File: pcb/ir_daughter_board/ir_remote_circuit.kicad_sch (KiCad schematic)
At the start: 12 parts, among them J2 Conn_01x12, J3 Conn_01x12, SW1 BOOT, SW2 RESET, U2 ESP32-WROOM-32E_(16MB)

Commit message: minor editorial changes
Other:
- moved on the sheet: C10, C9, D6, J2, J3, R8, R9, SW1, SW2

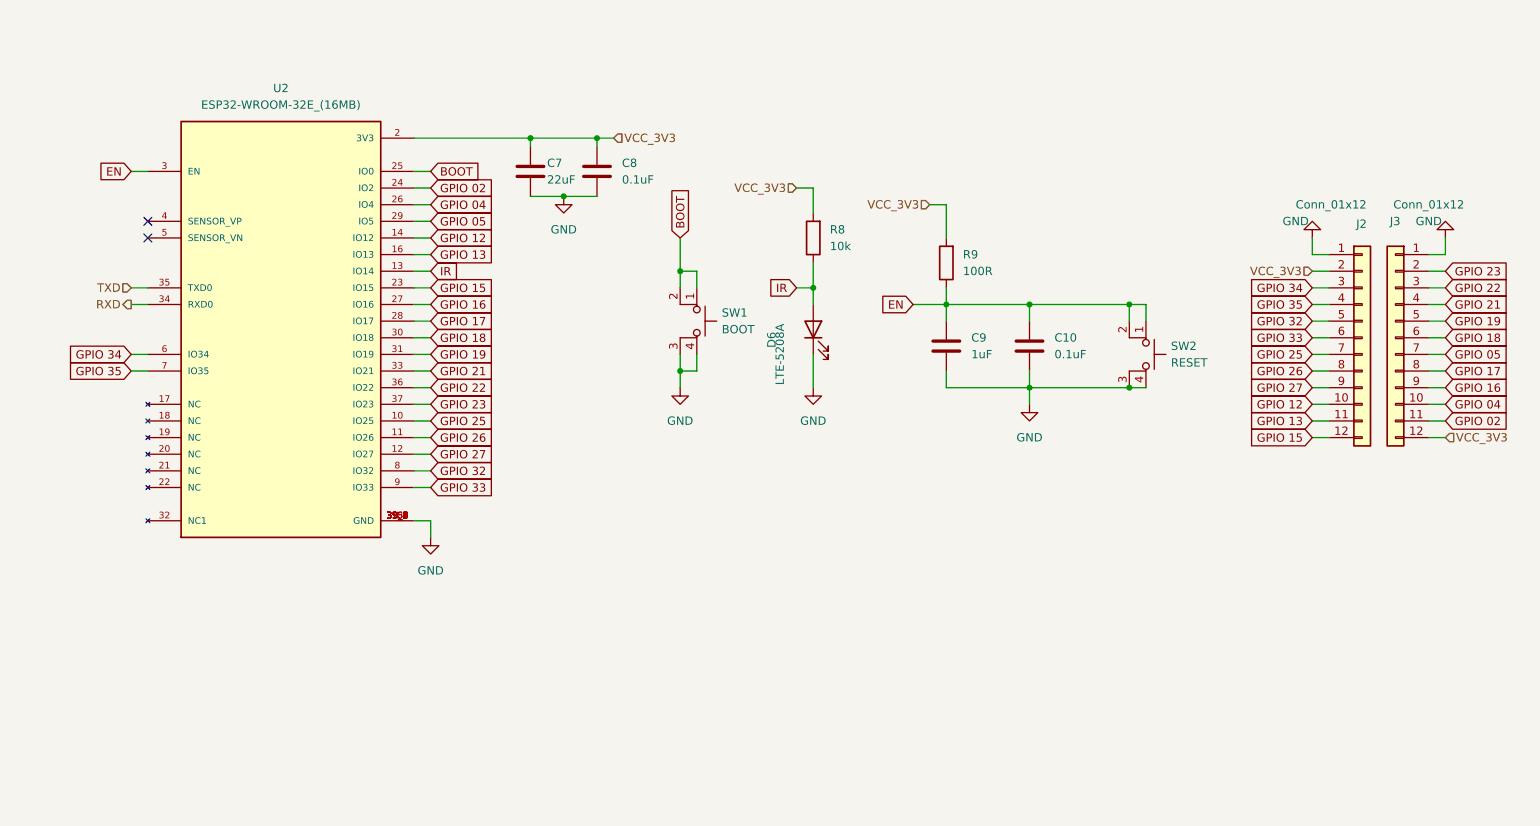
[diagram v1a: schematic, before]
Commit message: refined circuit with reddit comments
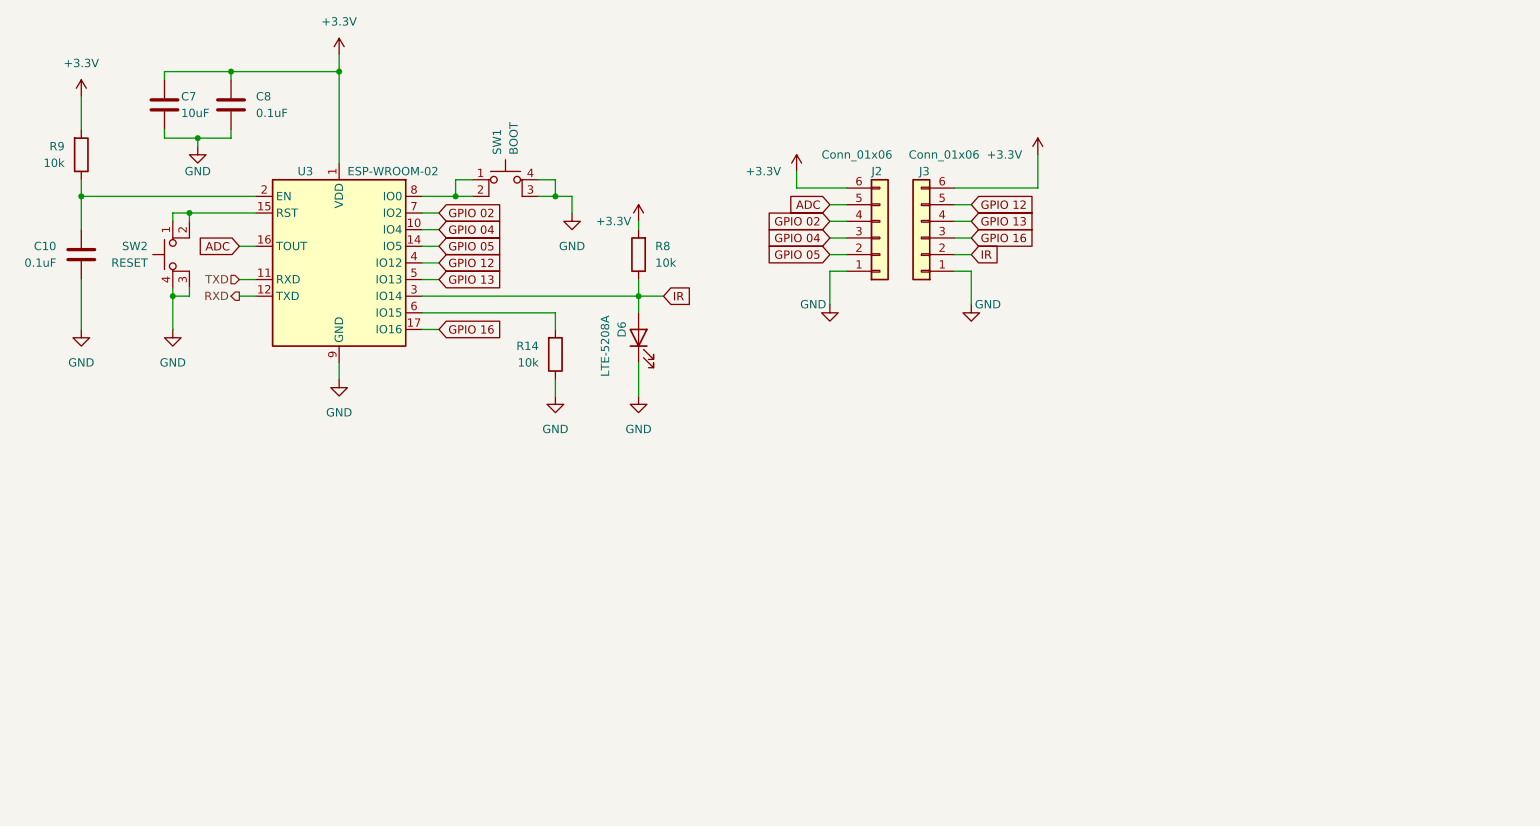
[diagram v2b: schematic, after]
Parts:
- removed C9: 1uF, Capacitor_SMD:C_0603_1608Metric, symbol Device:C
- removed J2, J3: Conn_01x12, Connector_PinHeader_2.54mm:PinHeader_1x12_P2.54mm_Vertical, symbol Connector_Generic:Conn_01x12
- removed U2: ESP32-WROOM-32E_(16MB), ESP32-WROOM-32E:MODULE_ESP32-WROOM-32E_(16MB), symbol ESP32-WROOM-32E:ESP32-WROOM-32E_(16MB)
- added J2, J3: Conn_01x06, Connector_PinHeader_2.54mm:PinHeader_1x06_P2.54mm_Vertical, symbol Connector_Generic:Conn_01x06
- added R14: 10k, Resistor_SMD:R_0603_1608Metric, symbol Device:R
- added U3: ESP-WROOM-02, RF_Module:ESP-WROOM-02, symbol RF_Module:ESP-WROOM-02
- C7: value 22uF -> 10uF
- R9: value 100R -> 10k
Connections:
- net GND: now also J2.1 (Pin_1), J3.1 (Pin_1), R14.1, U3.13 (GND), U3.18 (GND), U3.19 (GND), U3.9 (GND)
- net GPIO 02: now also J2.4 (Pin_4), U3.7 (IO2)
- net GPIO 04: now also J2.3 (Pin_3), U3.10 (IO4)
- net GPIO 05: now also J2.2 (Pin_2), U3.14 (IO5)
- net GPIO 12: now also J3.5 (Pin_5), U3.4 (IO12)
- net GPIO 13: now also J3.4 (Pin_4), U3.5 (IO13)
- net GPIO 16: now also J3.3 (Pin_3), U3.17 (IO16)
- net IR: now also J3.2 (Pin_2), U3.3 (IO14)
- net RXD: now also U3.12 (TXD)
- net TXD: now also U3.11 (RXD)
- net BOOT: no longer names the net of SW1.1, SW1.2
- net BOOT: now also U3.8 (IO0)
- net EN: no longer names the net of C10.1, R9.1
- net EN: now also U3.2 (EN); no longer SW2.1, SW2.2
- net VCC_3V3 renamed +3V3
- net +3V3: now also J2.6 (Pin_6), J3.6 (Pin_6), U3.1 (VDD)
- new net: SW2.1, SW2.2, U3.15 (RST)
- new net: R14.2, U3.6 (IO15)
- new net ADC: J2.5 (Pin_5), U3.16 (TOUT)
- no-connect marks 2 -> 0
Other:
- moved on the sheet: C10, C7, C8, D6, R8, R9, SW1, SW2

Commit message: updated schematic
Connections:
- net ADC: now also J3.3 (Pin_3); no longer J2.5 (Pin_5)
- net GND: no longer D6.1 (K)
- net GPIO 02: now also J2.5 (Pin_5); no longer J2.4 (Pin_4)
- net GPIO 04: now also J3.5 (Pin_5); no longer J2.3 (Pin_3)
- net GPIO 05: now also J3.4 (Pin_4); no longer J2.2 (Pin_2)
- net GPIO 12: now also J2.3 (Pin_3); no longer J3.5 (Pin_5)
- net GPIO 13: now also J2.4 (Pin_4); no longer J3.4 (Pin_4)
- net GPIO 16: now also J3.2 (Pin_2); no longer J3.3 (Pin_3)
- net IR: now also D6.1 (K), J2.2 (Pin_2); no longer D6.2 (A), J3.2 (Pin_2), R8.1
- new net: D6.2 (A), R8.1
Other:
- moved on the sheet: D6, R8

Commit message: minor update in PCB
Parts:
- C10, C8: value 0.1uF -> 100nF
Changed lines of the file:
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@@
   )
   (symbol (lib_id "Device:C") (at 48.26 81.28 0) (mirror y) (unit 1)
-    (in_bom yes) (on_board yes) (fields_autoplaced)
-    (property "Reference" "C10" (id 0) (at 44.45 80.0099 0)
-      (effects (font (size 1.27 1.27)) (justify left))
+    (in_bom yes) (on_board yes)
+    (property "Reference" "C10" (id 0) (at 41.275 80.01 0)
+      (effects (font (size 1.27 1.27)) (justify right))
     )
-    (property "Value" "0.1uF" (id 1) (at 44.45 82.5499 0)
-      (effects (font (size 1.27 1.27)) (justify left))
+    (property "Value" "100nF" (id 1) (at 39.37 82.55 0)
+      (effects (font (size 1.27 1.27)) (justify right))
     )
     (property "Footprint" "Capacitor_SMD:C_0603_1608Metric" (id 2) (at 47.2948 85.09 0)
@@
       (effects (font (size 1.27 1.27)) (justify left))
     )
-    (property "Value" "0.1uF" (id 1) (at 74.93 59.6899 0)
+    (property "Value" "100nF" (id 1) (at 74.93 59.6899 0)
       (effects (font (size 1.27 1.27)) (justify left))
     )

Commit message: minor updateds in references and values
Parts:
- D5: renamed from D6; value LTE-5208A -> IR-LED 940nm
- SW1: renamed from SW2; value RESET -> SW_MEC_5E
- SW2: renamed from SW1; value BOOT -> SW_MEC_5E
- renumbered C10 to C7, C7 to C8, C8 to C9, R9 to R11, R14 to R12, R8 to R13, U3 to U2
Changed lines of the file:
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@@
   (symbol (lib_id "power:+3.3V") (at 48.26 57.15 0) (unit 1)
     (in_bom yes) (on_board yes) (fields_autoplaced)
-    (property "Reference" "#PWR018" (id 0) (at 48.26 60.96 0)
+    (property "Reference" "#PWR020" (id 0) (at 48.26 60.96 0)
       (effects (font (size 1.27 1.27)) hide)
     )
@@
   (symbol (lib_id "power:GND") (at 48.26 92.71 0) (mirror y) (unit 1)
     (in_bom yes) (on_board yes) (fields_autoplaced)
-    (property "Reference" "#PWR012" (id 0) (at 48.26 99.06 0)
+    (property "Reference" "#PWR021" (id 0) (at 48.26 99.06 0)
       (effects (font (size 1.27 1.27)) hide)
     )
@@
   (symbol (lib_id "Device:C") (at 48.26 81.28 0) (mirror y) (unit 1)
     (in_bom yes) (on_board yes)
-    (property "Reference" "C10" (id 0) (at 41.275 80.01 0)
+    (property "Reference" "C7" (id 0) (at 41.275 80.01 0)
       (effects (font (size 1.27 1.27)) (justify right))
     )
@@
   (symbol (lib_id "Device:R") (at 133.35 69.85 180) (unit 1)
     (in_bom yes) (on_board yes) (fields_autoplaced)
-    (property "Reference" "R8" (id 0) (at 135.89 68.5799 0)
+    (property "Reference" "R13" (id 0) (at 135.89 68.5799 0)
       (effects (font (size 1.27 1.27)) (justify right))
     )
@@
   (symbol (lib_id "power:+3.3V") (at 194.31 66.04 0) (unit 1)
     (in_bom yes) (on_board yes)
-    (property "Reference" "#PWR024" (id 0) (at 194.31 69.85 0)
+    (property "Reference" "#PWR032" (id 0) (at 194.31 69.85 0)
       (effects (font (size 1.27 1.27)) hide)
     )
@@
   (symbol (lib_id "Device:R") (at 48.26 66.04 0) (mirror x) (unit 1)
     (in_bom yes) (on_board yes) (fields_autoplaced)
-    (property "Reference" "R9" (id 0) (at 45.72 64.7699 0)
+    (property "Reference" "R11" (id 0) (at 45.72 64.7699 0)
       (effects (font (size 1.27 1.27)) (justify right))
     )
@@
   )
   (symbol (lib_id "Switch:SW_MEC_5E") (at 64.77 81.28 90) (mirror x) (unit 1)
-    (in_bom yes) (on_board yes) (fields_autoplaced)
-    (property "Reference" "SW2" (id 0) (at 58.42 80.0099 90)
-      (effects (font (size 1.27 1.27)) (justify left))
-    )
-    (property "Value" "RESET" (id 1) (at 58.42 82.5499 90)
-      (effects (font (size 1.27 1.27)) (justify left))
+    (in_bom yes) (on_board yes)
+    (property "Reference" "SW1" (id 0) (at 55.88 80.01 90)
+      (effects (font (size 1.27 1.27)) (justify right))
+    )
+    (property "Value" "SW_MEC_5E" (id 1) (at 58.42 92.71 0)
+      (effects (font (size 1.27 1.27)) (justify right))
     )
     (property "Footprint" "Button_Switch_SMD:SW_SPST_Omron_B3FS-100xP" (id 2) (at 57.15 81.28 0)
@@
   (symbol (lib_id "Switch:SW_MEC_5E") (at 113.03 72.39 0) (unit 1)
     (in_bom yes) (on_board yes) (fields_autoplaced)
-    (property "Reference" "SW1" (id 0) (at 111.7599 66.04 90)
-      (effects (font (size 1.27 1.27)) (justify left))
-    )
-    (property "Value" "BOOT" (id 1) (at 114.2999 66.04 90)
-      (effects (font (size 1.27 1.27)) (justify left))
-    )
+    (property "Reference" "SW2" (id 0) (at 113.03 62.23 0))
+    (property "Value" "SW_MEC_5E" (id 1) (at 113.03 64.77 0))
     (property "Footprint" "Button_Switch_SMD:SW_SPST_Omron_B3FS-100xP" (id 2) (at 113.03 64.77 0)
       (effects (font (size 1.27 1.27)) hide)
@@
   (symbol (lib_id "Device:C") (at 71.12 58.42 0) (unit 1)
     (in_bom yes) (on_board yes) (fields_autoplaced)
-    (property "Reference" "C8" (id 0) (at 74.93 57.1499 0)
+    (property "Reference" "C9" (id 0) (at 74.93 57.1499 0)
       (effects (font (size 1.27 1.27)) (justify left))
     )
@@
   (symbol (lib_id "power:GND") (at 123.19 74.93 0) (unit 1)
     (in_bom yes) (on_board yes) (fields_autoplaced)
-    (property "Reference" "#PWR010" (id 0) (at 123.19 81.28 0)
+    (property "Reference" "#PWR027" (id 0) (at 123.19 81.28 0)
       (effects (font (size 1.27 1.27)) hide)
     )
@@
   (symbol (lib_id "power:+3.3V") (at 157.48 68.58 0) (unit 1)
     (in_bom yes) (on_board yes)
-    (property "Reference" "#PWR019" (id 0) (at 157.48 72.39 0)
+    (property "Reference" "#PWR029" (id 0) (at 157.48 72.39 0)
       (effects (font (size 1.27 1.27)) hide)
     )
@@
   (symbol (lib_id "Device:R") (at 120.65 96.52 0) (mirror x) (unit 1)
     (in_bom yes) (on_board yes) (fields_autoplaced)
-    (property "Reference" "R14" (id 0) (at 118.11 95.2499 0)
+    (property "Reference" "R12" (id 0) (at 118.11 95.2499 0)
       (effects (font (size 1.27 1.27)) (justify right))
     )
@@
   (symbol (lib_id "power:GND") (at 66.04 64.77 0) (unit 1)
     (in_bom yes) (on_board yes)
-    (property "Reference" "#PWR0102" (id 0) (at 66.04 71.12 0)
+    (property "Reference" "#PWR023" (id 0) (at 66.04 71.12 0)
       (effects (font (size 1.27 1.27)) hide)
     )
@@
   (symbol (lib_id "Device:C") (at 60.96 58.42 0) (unit 1)
     (in_bom yes) (on_board yes)
-    (property "Reference" "C7" (id 0) (at 63.5 57.15 0)
+    (property "Reference" "C8" (id 0) (at 63.5 57.15 0)
       (effects (font (size 1.27 1.27)) (justify left))
     )
@@
   (symbol (lib_id "power:GND") (at 120.65 102.87 0) (unit 1)
     (in_bom yes) (on_board yes) (fields_autoplaced)
-    (property "Reference" "#PWR020" (id 0) (at 120.65 109.22 0)
+    (property "Reference" "#PWR026" (id 0) (at 120.65 109.22 0)
       (effects (font (size 1.27 1.27)) hide)
     )
@@
   (symbol (lib_id "power:GND") (at 87.63 100.33 0) (unit 1)
     (in_bom yes) (on_board yes) (fields_autoplaced)
-    (property "Reference" "#PWR0101" (id 0) (at 87.63 106.68 0)
+    (property "Reference" "#PWR025" (id 0) (at 87.63 106.68 0)
       (effects (font (size 1.27 1.27)) hide)
     )
@@
   (symbol (lib_id "power:+3.3V") (at 87.63 50.8 0) (unit 1)
     (in_bom yes) (on_board yes) (fields_autoplaced)
-    (property "Reference" "#PWR021" (id 0) (at 87.63 54.61 0)
+    (property "Reference" "#PWR024" (id 0) (at 87.63 54.61 0)
       (effects (font (size 1.27 1.27)) hide)
     )
@@
   (symbol (lib_id "power:GND") (at 162.56 88.9 0) (mirror y) (unit 1)
     (in_bom yes) (on_board yes)
-    (property "Reference" "#PWR013" (id 0) (at 162.56 95.25 0)
+    (property "Reference" "#PWR030" (id 0) (at 162.56 95.25 0)
       (effects (font (size 1.27 1.27)) hide)
     )
@@
   (symbol (lib_id "Device:LED") (at 133.35 81.28 90) (unit 1)
     (in_bom yes) (on_board yes)
-    (property "Reference" "D6" (id 0) (at 130.81 80.01 0))
-    (property "Value" " LTE-5208A" (id 1) (at 128.27 82.55 0))
+    (property "Reference" "D5" (id 0) (at 130.81 80.01 0))
+    (property "Value" "IR-LED 940nm" (id 1) (at 128.27 78.74 0))
     (property "Footprint" "LED_THT:LED_D5.0mm" (id 2) (at 133.35 81.28 0)
       (effects (font (size 1.27 1.27)) hide)
@@
   (symbol (lib_id "power:GND") (at 62.23 92.71 0) (mirror y) (unit 1)
     (in_bom yes) (on_board yes) (fields_autoplaced)
-    (property "Reference" "#PWR08" (id 0) (at 62.23 99.06 0)
+    (property "Reference" "#PWR022" (id 0) (at 62.23 99.06 0)
       (effects (font (size 1.27 1.27)) hide)
     )
@@
   (symbol (lib_id "power:+3.3V") (at 133.35 63.5 0) (unit 1)
     (in_bom yes) (on_board yes)
-    (property "Reference" "#PWR022" (id 0) (at 133.35 67.31 0)
+    (property "Reference" "#PWR028" (id 0) (at 133.35 67.31 0)
       (effects (font (size 1.27 1.27)) hide)
     )
@@
   (symbol (lib_id "RF_Module:ESP-WROOM-02") (at 87.63 82.55 0) (unit 1)
     (in_bom yes) (on_board yes)
-    (property "Reference" "U3" (id 0) (at 81.28 68.58 0)
+    (property "Reference" "U2" (id 0) (at 81.28 68.58 0)
       (effects (font (size 1.27 1.27)) (justify left))
     )
@@
   (symbol (lib_id "power:GND") (at 184.15 88.9 0) (unit 1)
     (in_bom yes) (on_board yes)
-    (property "Reference" "#PWR023" (id 0) (at 184.15 95.25 0)
-      (effects (font (size 1.27 1.27)) hide)
-    )
+    (property "Reference" "#PWR031" (id 0) (at 184.15 95.25 0)
+      (effects (font (size 1.27 1.27)) hide)
+    )
